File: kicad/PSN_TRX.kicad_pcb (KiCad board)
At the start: 4 copper layers, 220 x 150 mm, 152 parts, among them IC1 LP2950L-5.0V, IC2 NJM2904, J1 PWR_IN, J2 SP-OUT, J3 RF-IN, J4 MIC-IN, J5 I2C_OUT, J6 Volume, J7 Volume, K1 G5V-2, Q1 3SK59, Q11 2SC1815, Q12 2SC1815, Q13 2SC1815, Q14 2SK439, Q15 2SC1815, Q17 2SC1815, Q2 2SC1923, Q3 2SC1815, Q4 2SC1815, Q5 2SC2120, Q6 2SA950, Q9 2SK439, T1 ST-71, U1 Si5351_DIP8, U2 AE-LCNV4-MOSFET, U3 LP2950-3.3_TO92

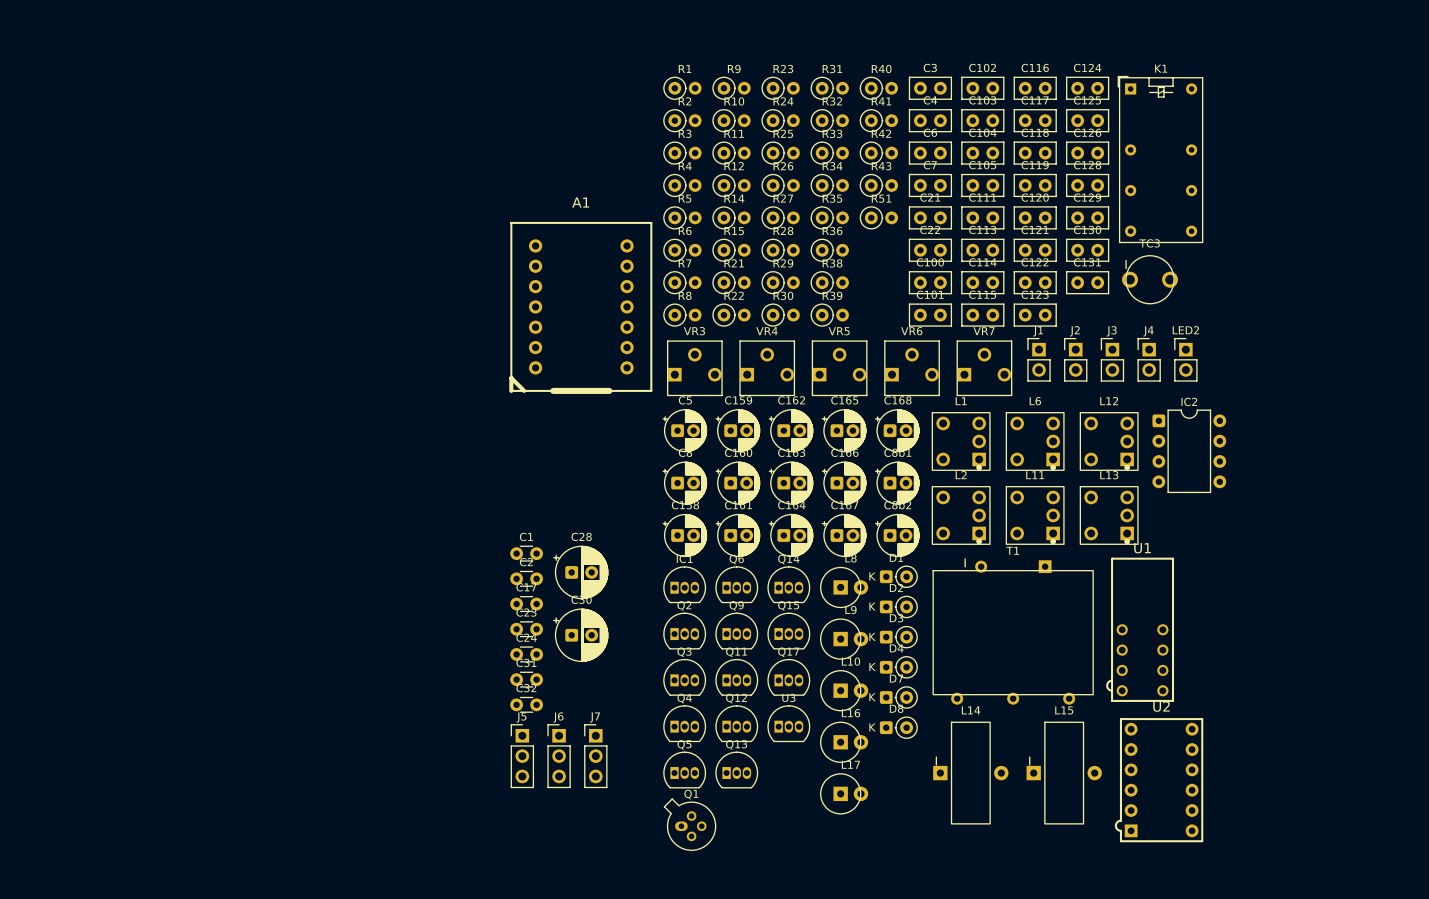
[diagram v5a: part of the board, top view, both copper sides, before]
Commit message: fix: U2フットプリントをDIP-12からDIP-8に修正
AE-Si5351Aモジュールは8ピン（左右各4ピン、7.62mm幅）であるが、
PCBにDIP-12_W7.62mm（12ピン）が誤って割り当てられていた。
回路図の設定（DIP-8_W7.62mm）と一致させるよう修正。
パッドUUID・位置・パス情報は既存のものを保持。

Co-Authored-By: Claude Sonnet 4.6 <noreply@anthropic.com>
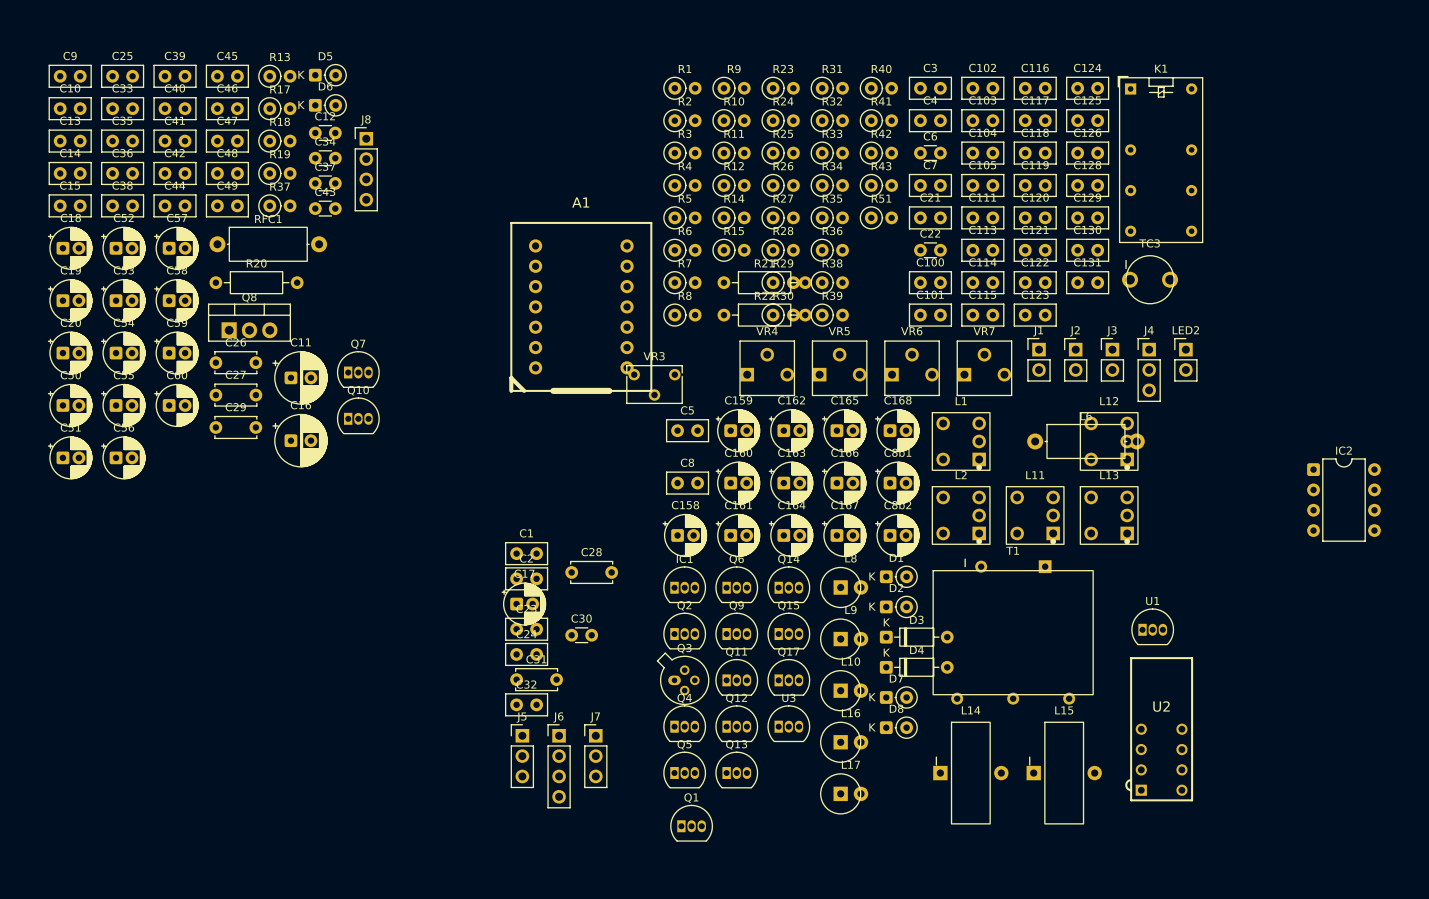
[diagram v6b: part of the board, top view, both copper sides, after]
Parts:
- added C10: 1u, Capacitor_THT:C_Disc_D5.0mm_W2.5mm_P2.50mm, F.Cu at (31.5, 44.6)
- added C11: 100u, Capacitor_THT:CP_Radial_D6.3mm_P2.50mm, F.Cu at (60.4, 78.2)
- added C12: 15p, Capacitor_THT:C_Disc_D3.0mm_W1.6mm_P2.50mm, F.Cu at (63.4, 47.6)
- added C13: 0.01u, Capacitor_THT:C_Disc_D5.0mm_W2.5mm_P2.50mm, F.Cu at (31.5, 48.6)
- added C14: 0.01u, Capacitor_THT:C_Disc_D5.0mm_W2.5mm_P2.50mm, F.Cu at (31.5, 52.7)
- added C15: 0.01u, Capacitor_THT:C_Disc_D5.0mm_W2.5mm_P2.50mm, F.Cu at (31.5, 56.7)
- added C16: 100u, Capacitor_THT:CP_Radial_D6.3mm_P2.50mm, F.Cu at (60.4, 86.1)
- added C18: 10u, Capacitor_THT:CP_Radial_D5.0mm_P2.00mm, F.Cu at (31.9, 62.0)
- added C19: 10u, Capacitor_THT:CP_Radial_D5.0mm_P2.00mm, F.Cu at (31.9, 68.6)
- added C20: 10u, Capacitor_THT:CP_Radial_D5.0mm_P2.00mm, F.Cu at (31.9, 75.1)
- added C25: 0.01u, Capacitor_THT:C_Disc_D5.0mm_W2.5mm_P2.50mm, F.Cu at (38.1, 40.5)
- added C26: 1000pF, Capacitor_THT:C_Disc_D5.0mm_W2.5mm_P5.00mm, F.Cu at (51.0, 76.3)
- added C27: 0.1uF, Capacitor_THT:C_Disc_D5.0mm_W2.5mm_P5.00mm, F.Cu at (51.0, 80.4)
- added C29: 100pF, Capacitor_THT:C_Disc_D5.0mm_W2.5mm_P5.00mm, F.Cu at (51.0, 84.4)
- added C33: 0.01u, Capacitor_THT:C_Disc_D5.0mm_W2.5mm_P2.50mm, F.Cu at (38.1, 44.6)
- added C34: 15p, Capacitor_THT:C_Disc_D3.0mm_W1.6mm_P2.50mm, F.Cu at (63.4, 50.8)
- added C35: 0.01u, Capacitor_THT:C_Disc_D5.0mm_W2.5mm_P2.50mm, F.Cu at (38.1, 48.6)
- added C36: 0.01u, Capacitor_THT:C_Disc_D5.0mm_W2.5mm_P2.50mm, F.Cu at (38.1, 52.7)
- added C37: 15p, Capacitor_THT:C_Disc_D3.0mm_W1.6mm_P2.50mm, F.Cu at (63.4, 53.9)
- added C38: 0.001u, Capacitor_THT:C_Disc_D5.0mm_W2.5mm_P2.50mm, F.Cu at (38.1, 56.7)
- added C39: 0.01u, Capacitor_THT:C_Disc_D5.0mm_W2.5mm_P2.50mm, F.Cu at (44.6, 40.5)
- added C40: 0.01u, Capacitor_THT:C_Disc_D5.0mm_W2.5mm_P2.50mm, F.Cu at (44.6, 44.6)
- added C41: 47PF, Capacitor_THT:C_Disc_D5.0mm_W2.5mm_P2.50mm, F.Cu at (44.6, 48.6)
- added C42: 47PF, Capacitor_THT:C_Disc_D5.0mm_W2.5mm_P2.50mm, F.Cu at (44.6, 52.7)
- added C43: 5p, Capacitor_THT:C_Disc_D3.0mm_W1.6mm_P2.50mm, F.Cu at (63.4, 57.1)
- added C44: 0.001u, Capacitor_THT:C_Disc_D5.0mm_W2.5mm_P2.50mm, F.Cu at (44.6, 56.7)
- added C45: 0.01u, Capacitor_THT:C_Disc_D5.0mm_W2.5mm_P2.50mm, F.Cu at (51.2, 40.5)
- added C46: 47PF, Capacitor_THT:C_Disc_D5.0mm_W2.5mm_P2.50mm, F.Cu at (51.2, 44.6)
- added C47: 47PF, Capacitor_THT:C_Disc_D5.0mm_W2.5mm_P2.50mm, F.Cu at (51.2, 48.6)
- added C48: 0.01u, Capacitor_THT:C_Disc_D5.0mm_W2.5mm_P2.50mm, F.Cu at (51.2, 52.7)
- added C49: 0.01u, Capacitor_THT:C_Disc_D5.0mm_W2.5mm_P2.50mm, F.Cu at (51.2, 56.7)
- added C50: 1u, Capacitor_THT:CP_Radial_D5.0mm_P2.00mm, F.Cu at (31.9, 81.7)
- added C51: 1u, Capacitor_THT:CP_Radial_D5.0mm_P2.00mm, F.Cu at (31.9, 88.2)
- added C52: 1u, Capacitor_THT:CP_Radial_D5.0mm_P2.00mm, F.Cu at (38.5, 62.0)
- added C53: 1u, Capacitor_THT:CP_Radial_D5.0mm_P2.00mm, F.Cu at (38.5, 68.6)
- added C54: 1u, Capacitor_THT:CP_Radial_D5.0mm_P2.00mm, F.Cu at (38.5, 75.1)
- added C55: 1u, Capacitor_THT:CP_Radial_D5.0mm_P2.00mm, F.Cu at (38.5, 81.7)
- added C56: 1u, Capacitor_THT:CP_Radial_D5.0mm_P2.00mm, F.Cu at (38.5, 88.2)
- added C57: 1u, Capacitor_THT:CP_Radial_D5.0mm_P2.00mm, F.Cu at (45.1, 62.0)
- added C58: 1u, Capacitor_THT:CP_Radial_D5.0mm_P2.00mm, F.Cu at (45.1, 68.6)
- added C59: 1u, Capacitor_THT:CP_Radial_D5.0mm_P2.00mm, F.Cu at (45.1, 75.1)
- added C60: 1u, Capacitor_THT:CP_Radial_D5.0mm_P2.00mm, F.Cu at (45.1, 81.7)
- added C9: 0.1u, Capacitor_THT:C_Disc_D5.0mm_W2.5mm_P2.50mm, F.Cu at (31.5, 40.5)
- added D5: 1N60, Diode_THT:D_DO-35_SOD27_P2.54mm_Vertical_CathodeUp, F.Cu at (63.4, 40.4)
- added D6: 1N60, Diode_THT:D_DO-35_SOD27_P2.54mm_Vertical_CathodeUp, F.Cu at (63.4, 44.2)
- added J8: MIC-IN, Connector_PinHeader_2.54mm:PinHeader_1x04_P2.54mm_Vertical, F.Cu at (69.8, 48.3)
- added Q10: 2SK439, Package_TO_SOT_THT:TO-92_Inline, F.Cu at (67.5, 83.3)
- added Q7: 2SK439, Package_TO_SOT_THT:TO-92_Inline, F.Cu at (67.5, 77.6)
- added Q8: 2SC1971, Package_TO_SOT_THT:TO-220-3_Vertical, F.Cu at (52.6, 72.3)
- added R13: 120, Resistor_THT:R_Axial_DIN0207_L6.3mm_D2.5mm_P2.54mm_Vertical, F.Cu at (57.7, 40.5)
- added R17: 100k, Resistor_THT:R_Axial_DIN0207_L6.3mm_D2.5mm_P2.54mm_Vertical, F.Cu at (57.7, 44.6)
- added R18: 51, Resistor_THT:R_Axial_DIN0207_L6.3mm_D2.5mm_P2.54mm_Vertical, F.Cu at (57.7, 48.6)
- added R19: 20k, Resistor_THT:R_Axial_DIN0207_L6.3mm_D2.5mm_P2.54mm_Vertical, F.Cu at (57.7, 52.7)
- added R20: 10, Resistor_THT:R_Axial_DIN0207_L6.3mm_D2.5mm_P10.16mm_Horizontal, F.Cu at (51.0, 66.3)
- added R37: 330, Resistor_THT:R_Axial_DIN0207_L6.3mm_D2.5mm_P2.54mm_Vertical, F.Cu at (57.7, 56.7)
- added RFC1: 10uH, Inductor_THT:L_Axial_L9.5mm_D4.0mm_P12.70mm_Horizontal_Fastron_SMCC, F.Cu at (51.2, 61.5)
- C1, C2: value 15p -> 1u; footprint Capacitor_THT:C_Disc_D3.0mm_W1.6mm_P2.50mm -> Capacitor_THT:C_Disc_D5.0mm_W2.5mm_P2.50mm
- C17: value 15p -> 10u; footprint Capacitor_THT:C_Disc_D3.0mm_W1.6mm_P2.50mm -> Capacitor_THT:CP_Radial_D5.0mm_P2.00mm
- C22: value 0.001u -> 15p; footprint Capacitor_THT:C_Disc_D5.0mm_W2.5mm_P2.50mm -> Capacitor_THT:C_Disc_D3.0mm_W1.6mm_P2.50mm
- C23, C24: value 15p -> 0.01u; footprint Capacitor_THT:C_Disc_D3.0mm_W1.6mm_P2.50mm -> Capacitor_THT:C_Disc_D5.0mm_W2.5mm_P2.50mm
- C28: value 100u -> 100pF; footprint Capacitor_THT:CP_Radial_D6.3mm_P2.50mm -> Capacitor_THT:C_Disc_D5.0mm_W2.5mm_P5.00mm
- C3: value 0.001u -> 0.1u
- C30: value 100u -> 15p; footprint Capacitor_THT:CP_Radial_D6.3mm_P2.50mm -> Capacitor_THT:C_Disc_D3.0mm_W1.6mm_P2.50mm
- C31: value 15p -> 22pF; footprint Capacitor_THT:C_Disc_D3.0mm_W1.6mm_P2.50mm -> Capacitor_THT:C_Disc_D5.0mm_W2.5mm_P5.00mm
- C32: value 5p -> 0.01u; footprint Capacitor_THT:C_Disc_D3.0mm_W1.6mm_P2.50mm -> Capacitor_THT:C_Disc_D5.0mm_W2.5mm_P2.50mm
- C5, C8: value 10u -> 1u; footprint Capacitor_THT:CP_Radial_D5.0mm_P2.00mm -> Capacitor_THT:C_Disc_D5.0mm_W2.5mm_P2.50mm
- C6: value 0.1u -> 15p; footprint Capacitor_THT:C_Disc_D5.0mm_W2.5mm_P2.50mm -> Capacitor_THT:C_Disc_D3.0mm_W1.6mm_P2.50mm
- C7: value 0.1u -> 0.01u
- D3, D4: value 1N60 -> 1N4148; footprint Diode_THT:D_DO-35_SOD27_P2.54mm_Vertical_CathodeUp -> Diode_THT:D_DO-35_SOD27_P7.62mm_Horizontal
- J1: value PWR_IN -> RF_IN
- J3: value RF-IN -> PWR_IN
- J4: value MIC-IN -> Volume; footprint Connector_PinHeader_2.54mm:PinHeader_1x02_P2.54mm_Vertical -> Connector_PinHeader_2.54mm:PinHeader_1x03_P2.54mm_Vertical
- J5: value I2C_OUT -> Volume
- J6: value Volume -> Conn_01x04; footprint Connector_PinHeader_2.54mm:PinHeader_1x03_P2.54mm_Vertical -> Connector_PinHeader_2.54mm:PinHeader_1x04_P2.54mm_Vertical
- J7: value Volume -> I2C_OUT
- L10: value 1mH -> 100nH
- L11: value 7T50 -> 100nH
- L12, L13: value 7T50 -> 1mH
- L14: value T-50-10 18T/0.4mm -> 15mH
- L6: value 7T50 -> 47nH; footprint PSN_TRX:L_FCZ07S_CT -> Inductor_THT:L_Axial_L9.5mm_D4.0mm_P12.70mm_Horizontal_Fastron_SMCC
- L8: value 15mH -> 7T50
- L9: value 1mH -> 7T50
- Q1: value 3SK59 -> 2SC2120; footprint Package_TO_SOT_THT:TO-72-4 -> Package_TO_SOT_THT:TO-92_Inline
- Q14, Q9: value 2SK439 -> 2SC1815
- Q2: value 2SC1923 -> 2SC1815
- Q3: value 2SC1815 -> 3SK59; footprint Package_TO_SOT_THT:TO-92_Inline -> Package_TO_SOT_THT:TO-72-4
- Q4: value 2SC1815 -> 2SC1923
- Q5: value 2SC2120 -> 2SC1815
- R1: value 120 -> 100k
- R10: value 1k -> 4.7
- R11, R12: value 10k -> 1k
- R14: value 20k -> 100
- R15: value 100 -> 20k
- R2: value 1M -> 100k
- R21: value 47 -> 10; footprint Resistor_THT:R_Axial_DIN0207_L6.3mm_D2.5mm_P2.54mm_Vertical -> Resistor_THT:R_Axial_DIN0207_L6.3mm_D2.5mm_P10.16mm_Horizontal
- R22: value 1k -> 470; footprint Resistor_THT:R_Axial_DIN0207_L6.3mm_D2.5mm_P2.54mm_Vertical -> Resistor_THT:R_Axial_DIN0207_L6.3mm_D2.5mm_P10.16mm_Horizontal
- R23: value 100k -> 51
- R24: value 1k -> 4.7k
- R25: value 330 -> 1k
- R26: value 10k -> 51
- R27: value 10k -> 47
- R28: value 1M -> 100
- R29: value 4.7k -> 47
- R3: value 4.7 -> 1.5k
- R30: value 330 -> 4.7k
- R31: value 1M -> 10k
- R32: value 4.7k -> 1k
- R33, R40, R9: value 1k -> 1M
- R34: value 47 -> 10k
- R35: value 20k -> 100k
- R36: value 51 -> 1k
- R39: value 51 -> 330
- R4: value 1.5k -> 1k
- R41: value 100 -> 1k
- R5: value 1k -> 330
- R6, R8: value 100k -> 10k
- U1: value Si5351_DIP8 -> LP2950-3.3_TO92; footprint PSN_TRX:DIP-8_W7.62mm -> Package_TO_SOT_THT:TO-92_Inline
- U2: value AE-LCNV4-MOSFET -> Si5351_DIP8; footprint PSN_TRX:DIP-12_W7.62mm -> PSN_TRX:DIP-8_W7.62mm
- VR3: value 10k -> 500; footprint PSN_TRX:Potentiometer_TOCOS_GF063P_Vertical -> Potentiometer_THT:Potentiometer_Bourns_3266W_Vertical
- VR5: value 1k -> 500
- VR6: value 500 -> 1k
- moved IC2 20.3 mm to (188.2, 89.7)
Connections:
- A1 pad 1: (no net) -> Net-(A1-D0/A0)
- A1 pad 10: (no net) -> unconnected-(A1-3V3-Pad10)
- A1 pad 11: (no net) -> unconnected-(A1-D10/MOSI-Pad11)
- A1 pad 12: (no net) -> unconnected-(A1-D9/MISO-Pad12)
- A1 pad 13: (no net) -> unconnected-(A1-D8/SCK-Pad13)
- A1 pad 14: (no net) -> unconnected-(A1-D7/RX-Pad14)
- A1 pad 2: (no net) -> Net-(A1-D1/A1)
- A1 pad 3: (no net) -> Net-(A1-D2/A2)
- A1 pad 4: (no net) -> unconnected-(A1-D3/A3-Pad4)
- A1 pad 5: (no net) -> Net-(A1-D4/SDA)
- A1 pad 6: (no net) -> Net-(A1-D5/SCL)
- A1 pad 7: (no net) -> unconnected-(A1-D6/TX-Pad7)
- A1 pad 8: (no net) -> +5V
- A1 pad 9: (no net) -> GND
- C1 pad 1: Net-(L1-SA) -> Net-(Q2-C)
- C1 pad 2: GND -> Net-(C1-Pad2)
- C17 pad 1: Net-(L6-SA) -> +9V
- C17 pad 2: Net-(L6-SB) -> GND
- C2 pad 1: Net-(L2-AA) -> Net-(Q5-C)
- C2 pad 2: +9V -> Net-(C2-Pad2)
- C21 pad 1: Net-(C114-Pad2) -> Net-(Q4-E)
- C21 pad 2: Net-(C21-Pad2) -> Net-(L3-AA)
- C22 pad 1: Net-(C22-Pad1) -> Net-(L3-SA)
- C22 pad 2: Net-(C22-Pad2) -> Net-(L3-SB)
- C23 pad 1: Net-(D1-A) -> Net-(L3-SB)
- C23 pad 2: Net-(D2-K) -> GND
- C24 pad 1: Net-(L12-SA) -> Net-(Q7-G)
- C24 pad 2: Net-(L12-SB) -> Net-(C24-Pad2)
- C28 pad 1: Net-(Q5-C) -> Net-(Q8-C)
- C28 pad 2: /PHONE -> Net-(C28-Pad2)
- C3 pad 1: Net-(Q2-E) -> Net-(C2-Pad2)
- C3 pad 2: Net-(L6-AA) -> GND
- C30 pad 1: Net-(Q6-E) -> Net-(L7-SA)
- C30 pad 2: GND -> Net-(L7-SB)
- C31 pad 1: Net-(L13-SA) -> Net-(Q8-B)
- C31 pad 2: Net-(L12-SB) -> GND
- C32 pad 1: Net-(C32-Pad1) -> Net-(L7-SB)
- C32 pad 2: Net-(D7-A) -> GND
- C4 pad 1: Net-(C104-Pad2) -> Net-(Q2-B)
- C5 pad 1: +9V -> Net-(J4-Pin_2)
- C5 pad 2: GND -> Net-(Q1-B)
- C6 pad 1: Net-(Q4-B) -> Net-(L1-AA)
- C6 pad 2: GND -> +9V
- C7 pad 1: Net-(Q4-E) -> Net-(L1-SA)
- C7 pad 2: GND -> Net-(Q4-B)
- C8 pad 1: +9V -> Net-(Q4-C)
- C8 pad 2: GND -> Net-(Q5-B)
- D3 pad 2: Net-(D1-A) -> Net-(D3-A)
- D4 pad 1: Net-(D2-K) -> Net-(D3-A)
- D4 pad 2: Net-(D4-A) -> GND
- D7 pad 1: Net-(D7-K) -> Net-(D2-K)
- D8 pad 1: Net-(D7-A) -> Net-(D6-A)
- IC2 pad 1: Net-(C158-Pad2) -> Net-(C54-Pad2)
- J4 pad 2: GND -> Net-(J4-Pin_2)
- J5 pad 1: Net-(J5-SDA) -> Net-(J5-Pin_1)
- J5 pad 2: Net-(J5-SCL) -> Net-(J5-Pin_2)
- J6 pad 1: Net-(J6-Pin_1) -> Net-(A1-D0/A0)
- J6 pad 2: Net-(J6-Pin_2) -> Net-(A1-D1/A1)
- J6 pad 3: GND -> Net-(A1-D2/A2)
- J7 pad 1: Net-(J7-Pin_1) -> Net-(A1-D4/SDA)
- J7 pad 2: Net-(J7-Pin_2) -> Net-(A1-D5/SCL)
- K1 pad 1: +5V -> unconnected-(K1-Pad1)
- K1 pad 6: Net-(L1-AA) -> Net-(L2-AA)
- K1 pad 8: Net-(C32-Pad1) -> Net-(C43-Pad1)
- K1 pad 9: Net-(L12-SB) -> Net-(L7-SB)
- L1 pad 5: GND -> +9V
- L10 pad 1: Net-(C22-Pad2) -> Net-(C39-Pad1)
- L10 pad 2: Net-(C124-Pad1) -> Net-(C41-Pad2)
- L11 pad 1: Net-(D1-A) -> Net-(C45-Pad1)
- L11 pad 2: unconnected-(L11-CT-Pad2) -> Net-(C46-Pad2)
- L11 pad 3: Net-(D2-K) -> (no net)
- L11 pad 4: Net-(L11-AA) -> (no net)
- L11 pad 5: GND -> (no net)
- L12 pad 1: Net-(L12-SA) -> Net-(C44-Pad2)
- L12 pad 2: unconnected-(L12-CT-Pad2) -> Net-(C48-Pad1)
- L12 pad 3: Net-(L12-SB) -> (no net)
- L12 pad 4: Net-(L12-AA) -> (no net)
- L12 pad 5: GND -> (no net)
- L13 pad 1: Net-(L13-SA) -> Net-(C38-Pad2)
- L13 pad 2: Net-(L13-CT) -> Net-(C49-Pad1)
- L13 pad 3: Net-(L12-SB) -> (no net)
- L13 pad 4: Net-(L13-AA) -> (no net)
- L13 pad 5: GND -> (no net)
- L14 pad 1: Net-(L14-Pad1) -> Net-(C52-Pad2)
- L14 pad 2: Net-(L13-AA) -> Net-(C53-Pad1)
- L2 pad 5: +9V -> GND
- L6 pad 1: Net-(L6-SA) -> Net-(C29-Pad2)
- L6 pad 2: unconnected-(L6-CT-Pad2) -> Net-(Q8-B)
- L8 pad 1: Net-(C162-Pad2) -> Net-(L8-SA)
- L8 pad 2: Net-(C159-Pad1) -> unconnected-(L8-CT-Pad2)
- L9 pad 1: Net-(C21-Pad2) -> Net-(D1-A)
- L9 pad 2: Net-(C120-Pad1) -> unconnected-(L9-CT-Pad2)
- LED2 pad 2: Net-(L12-SB) -> Net-(L7-SB)
- Q1 pad 1: Net-(L2-AA) -> Net-(Q1-B)
- Q1 pad 2: Net-(Q1-S) -> Net-(Q1-C)
- Q1 pad 3: Net-(L1-SA) -> GND
- Q11 pad 1: Net-(Q11-B) -> Net-(D6-K)
- Q11 pad 2: Net-(Q11-C) -> Net-(LED2-K)
- Q11 pad 3: Net-(Q11-E) -> GND
- Q12 pad 2: Net-(L13-CT) -> Net-(Q12-C)
- Q14 pad 1: Net-(L11-AA) -> Net-(Q14-B)
- Q14 pad 2: Net-(L12-SA) -> Net-(Q14-C)
- Q14 pad 3: Net-(Q14-S) -> Net-(Q14-E)
- Q3 pad 1: Net-(Q3-B) -> Net-(L1-AA)
- Q3 pad 2: Net-(Q3-C) -> Net-(Q3-S)
- Q3 pad 3: GND -> Net-(L2-SA)
- Q6 pad 2: Net-(Q5-C) -> Net-(Q1-C)
- Q9 pad 1: Net-(Q9-G) -> Net-(Q9-B)
- Q9 pad 2: Net-(L6-SA) -> Net-(L7-CT)
- Q9 pad 3: Net-(Q9-S) -> Net-(Q9-E)
- R1 pad 1: Net-(Q1-S) -> Net-(Q2-B)
- R1 pad 2: GND -> Net-(Q2-C)
- R10 pad 1: Net-(Q4-C) -> Net-(Q4-E)
- R10 pad 2: +9V -> GND
- R11 pad 1: Net-(Q5-B) -> Net-(Q4-C)
- R11 pad 2: Net-(Q5-C) -> +9V
- R12 pad 2: Net-(Q6-B) -> +9V
- R14 pad 1: Net-(J7-Pin_1) -> Net-(Q6-E)
- R15 pad 1: Net-(Q6-E) -> Net-(J5-Pin_1)
- R2 pad 1: Net-(Q2-B) -> Net-(Q5-B)
- R2 pad 2: +9V -> Net-(Q5-C)
- R21 pad 1: Net-(C114-Pad2) -> Net-(Q8-B)
- R21 pad 2: GND -> Net-(R21-Pad2)
- R22 pad 1: Net-(L12-SB) -> Net-(L7-SB)
- R22 pad 2: Net-(J4-Pin_1) -> Net-(R22-Pad2)
- R23 pad 1: Net-(Q11-C) -> Net-(Q9-E)
- R23 pad 2: Net-(Q11-B) -> GND
- R24 pad 1: Net-(L12-SB) -> Net-(Q9-B)
- R24 pad 2: Net-(Q11-C) -> GND
- R25 pad 1: Net-(Q11-E) -> Net-(LED2-K)
- R25 pad 2: GND -> Net-(L7-SB)
- R26 pad 1: Net-(IC2A-+) -> Net-(Q10-S)
- R26 pad 2: Net-(C164-Pad1) -> GND
- R27 pad 1: Net-(C158-Pad2) -> Net-(C24-Pad2)
- R27 pad 2: Net-(IC2A-+) -> GND
- R28 pad 1: Net-(Q13-C) -> Net-(D6-K)
- R28 pad 2: Net-(Q13-B) -> GND
- R29 pad 1: Net-(L12-SB) -> Net-(C44-Pad1)
- R29 pad 2: Net-(Q13-C) -> GND
- R3 pad 1: Net-(Q2-E) -> Net-(C2-Pad2)
- R3 pad 2: GND -> Net-(Q2-B)
- R30 pad 1: Net-(Q13-E) -> Net-(L7-SB)
- R30 pad 2: GND -> Net-(Q12-C)
- R31 pad 1: Net-(Q17-C) -> Net-(C54-Pad2)
- R31 pad 2: Net-(Q17-B) -> Net-(IC2A-+)
- R32 pad 1: Net-(L12-SB) -> Net-(L7-SB)
- R32 pad 2: Net-(Q17-C) -> Net-(Q13-C)
- R33 pad 1: Net-(Q17-E) -> Net-(Q12-C)
- R33 pad 2: GND -> Net-(Q12-B)
- R34 pad 1: Net-(C22-Pad1) -> Net-(IC2A-+)
- R34 pad 2: GND -> Net-(C51-Pad1)
- R35 pad 1: Net-(L12-SB) -> Net-(Q13-C)
- R35 pad 2: Net-(Q12-B) -> Net-(Q13-B)
- R36 pad 1: Net-(Q14-S) -> Net-(L7-SB)
- R36 pad 2: GND -> Net-(J8-Pin_2)
- R38 pad 1: Net-(Q12-B) -> Net-(L7-SB)
- R38 pad 2: GND -> Net-(Q14-C)
- R39 pad 1: Net-(Q12-E) -> Net-(Q13-E)
- R4 pad 1: Net-(C104-Pad2) -> Net-(Q2-C)
- R4 pad 2: Net-(Q4-B) -> +9V
- R40 pad 1: Net-(LED2-K) -> Net-(Q14-C)
- R40 pad 2: Net-(L12-SB) -> Net-(Q14-B)
- R41 pad 1: Net-(D7-K) -> Net-(Q14-E)
- R5 pad 1: Net-(Q2-C) -> Net-(C1-Pad2)
- R5 pad 2: +9V -> Net-(J4-Pin_1)
- R6 pad 1: Net-(Q3-B) -> Net-(Q1-B)
- R6 pad 2: Net-(Q3-C) -> Net-(Q1-C)
- R7 pad 1: Net-(Q3-C) -> Net-(Q2-E)
- R7 pad 2: +9V -> GND
- R8 pad 1: Net-(Q4-B) -> Net-(Q1-C)
- R8 pad 2: Net-(Q4-C) -> Net-(Q6-B)
- R9 pad 1: Net-(Q4-E) -> Net-(Q4-B)
- R9 pad 2: GND -> +9V
- U1 pad 1: unconnected-(U1-VDDO-Pad1)_1 -> Net-(U1-VO)
- U1 pad 2: Net-(J5-SCL) -> GND
- U1 pad 3: Net-(J5-SDA) -> +5V
- U2 pad 1: Net-(A1-A4/SDA) -> (no net)
- U2 pad 2: Net-(A1-A5/SCL) -> (no net)
- U2 pad 3: GND -> (no net)
- U2 pad 4: +5V -> (no net)
- U2 pad 5: unconnected-(U2-HV3-Pad5) -> (no net)
- U2 pad 6: unconnected-(U2-HV4-Pad6) -> (no net)
- U2 pad 7: unconnected-(U2-LV4-Pad7) -> (no net)
- U2 pad 8: unconnected-(U2-LV3-Pad8) -> (no net)
- VR3 pad 1: Net-(IC2A--) -> Net-(R22-Pad2)
- VR3 pad 2: Net-(C164-Pad1) -> Net-(R21-Pad2)
- VR3 pad 3: Net-(C164-Pad1) -> Net-(D3-K)
- VR4 pad 2: Net-(C21-Pad2) -> Net-(C38-Pad2)
- VR5 pad 1: Net-(D3-K) -> Net-(C24-Pad2)
- VR5 pad 2: Net-(C22-Pad2) -> Net-(C41-Pad2)
- VR5 pad 3: Net-(D4-A) -> Net-(C41-Pad2)
- VR6 pad 1: Net-(C114-Pad2) -> Net-(D5-K)
- VR6 pad 2: Net-(C129-Pad2) -> Net-(C44-Pad2)
- VR6 pad 3: Net-(C129-Pad2) -> Net-(D7-A)
- VR7 pad 1: Net-(C22-Pad1) -> Net-(C44-Pad1)
- VR7 pad 2: Net-(C130-Pad2) -> Net-(C46-Pad2)
- VR7 pad 3: Net-(C130-Pad2) -> Net-(C46-Pad2)
